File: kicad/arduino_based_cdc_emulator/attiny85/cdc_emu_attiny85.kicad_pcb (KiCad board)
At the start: 2 copper layers, 15.6 x 13 mm, 14 parts, among them IC1 ATTINY85-S, P1 CONN_01X05, P2 CONN_01X03, U1 AP1117D50, U2 LM78L05ACZ

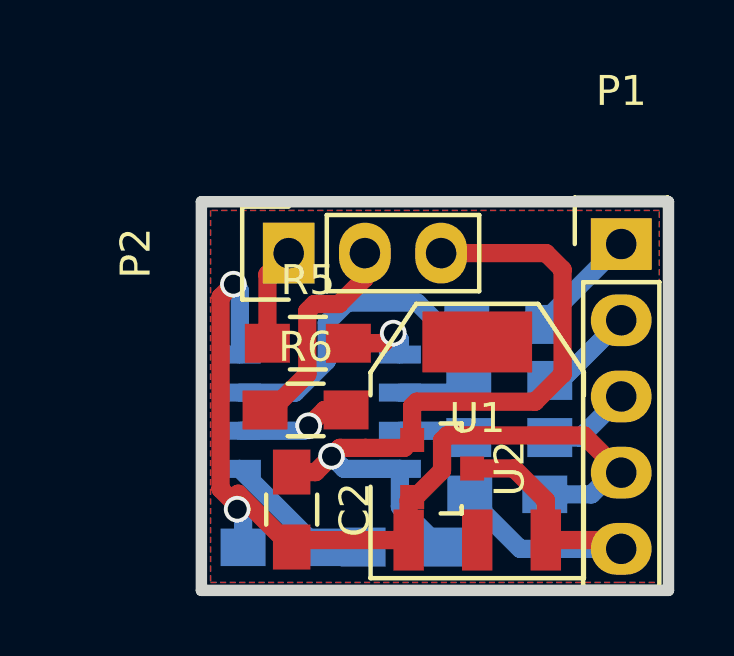
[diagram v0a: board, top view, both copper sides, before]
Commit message: fix 78L05 pinout, 5V connection from U1
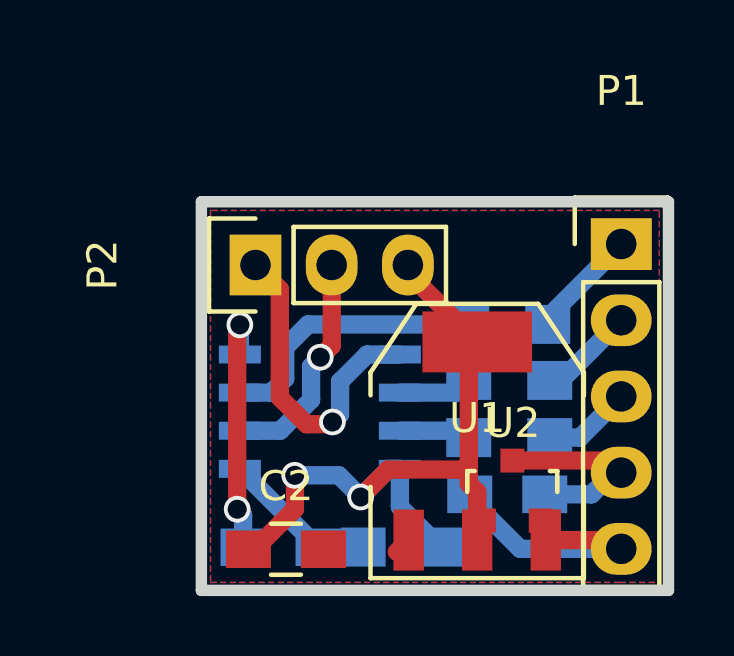
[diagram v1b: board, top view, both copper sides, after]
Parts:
- removed R5, R6: 3k3, Resistors_SMD:R_0805_HandSoldering
- moved U2 2.45 mm to (188.4, 101.6), turned to 0 degrees
- moved C2 1.33 mm to (180.8, 103.6), turned to 0 degrees
- moved P2 1.18 mm to (179.8, 94.1)
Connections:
- IC1 pad 2: Net-(IC1-Pad2) -> /TX
- IC1 pad 5: Net-(IC1-Pad5) -> /MOSI
- U1 pad 4: (no net) -> +5V
- U2 pad 2: GND -> +12V
- U2 pad 3: +12V -> GND
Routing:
- net GND: track 32.0 -> 15.7 mm
- net /MOSI: track 3.30 -> 10.7 mm, vias 0 -> 1
- net +12V: track 12.7 -> 8.52 mm
- net Net-(IC1-Pad2): track 3.83 -> 0.00 mm, vias 1 -> 0
- net Net-(IC1-Pad5): track 2.44 -> 0.00 mm, vias 1 -> 0
- net Net-(C3-Pad1): track 3.70 -> 5.20 mm
- net Net-(IC1-Pad3): track 9.85 -> 9.12 mm
- net +5V: track 24.6 -> 25.1 mm, vias 1 -> 2
- net /TX: track 7.21 -> 7.58 mm, vias 0 -> 1

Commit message: right package for attiny85
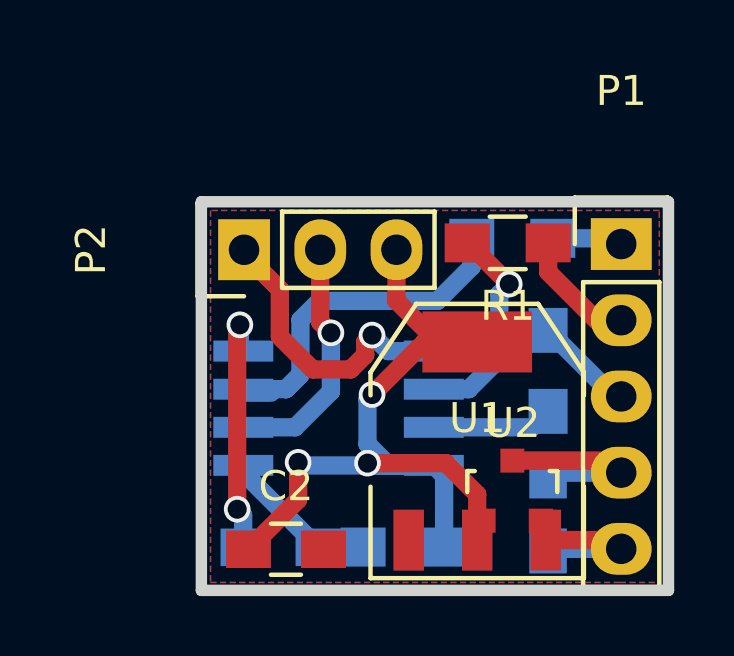
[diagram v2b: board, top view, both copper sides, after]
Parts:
- IC1: footprint SO8E -> my_modules:SOIC-8-N_wide_pads
- R1: moved to F.Cu
- moved R1 4.58 mm to (188.2, 93.4)
- moved R3 2.87 mm to (188.4, 93.2)
- moved R2 2.57 mm to (189.6, 97.6), turned to 270 degrees
- moved C1 1.50 mm to (189.6, 102.4), turned to 90 degrees
- moved P2 0.63 mm to (179.4, 93.6)
- moved IC1 0.63 mm to (182.6, 98.9)
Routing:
- net +5V: track 25.1 -> 33.0 mm, vias 2 -> 3
- net Net-(IC1-Pad6): track 2.46 -> 7.20 mm, vias 0 -> 1
- net Net-(IC1-Pad3): track 9.12 -> 13.0 mm
- net +12V: track 8.52 -> 5.10 mm
- net Net-(IC1-Pad7): track 2.39 -> 4.03 mm
- net /MOSI: track 10.7 -> 9.25 mm
- net /DataOut: track 3.69 -> 2.36 mm
- net /DataIn: track 3.21 -> 4.07 mm
- net /TX: track 7.58 -> 8.29 mm
- net GND: track 15.7 -> 15.1 mm

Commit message: updates
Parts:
- IC1: footprint my_modules:SOIC-8-N_wide_pads -> Housings_SOIC.pretty:SOIJ-8_5.3x5.3mm_Pitch1.27mm
- moved IC1 0.31 mm to (182.9, 98.9), turned to 0 degrees
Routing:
- net Net-(C3-Pad1): track 5.20 -> 9.06 mm
- net +5V: track 33.0 -> 32.1 mm
- net Net-(IC1-Pad3): track 13.0 -> 13.6 mm
